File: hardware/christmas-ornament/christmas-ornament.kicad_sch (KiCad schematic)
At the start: 21 parts, among them SW1 SW_Push, U1 ATtiny84A-SS

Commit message: designed basic pcb shape and routing (not finished)
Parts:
- added J1, J2, J3, J4, J5: Conn_01x01_Pin, TestPoint:TestPoint_Pad_D1.5mm, symbol Connector:Conn_01x01_Pin
- BT1: footprint (none) -> Battery:BatteryHolder_Keystone_1060_1x2032
- C1, C2: footprint (none) -> Capacitor_SMD:C_0805_2012Metric
- D1, D2, D3, D4, D5, D6, D7, D8: footprint (none) -> LED_THT:LED_D5.0mm
- R1, R2, R3, R4, R5, R6, R7, R8: footprint (none) -> Resistor_SMD:R_0805_2012Metric
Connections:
- net GND: now also J2.1 (Pin_1)
- net at BT1.1 (+), C1.1, C2.1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: now also J1.1 (Pin_1)
- net at R5.1, R6.1, U1.7 (PA6): now also J3.1 (Pin_1)
- net at U1.4 (~{RESET}/PB3): now also J5.1 (Pin_1)
- net at U1.9 (PA4): now also J4.1 (Pin_1)
- no-connect marks 7 -> 5
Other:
- moved on the sheet: SW1

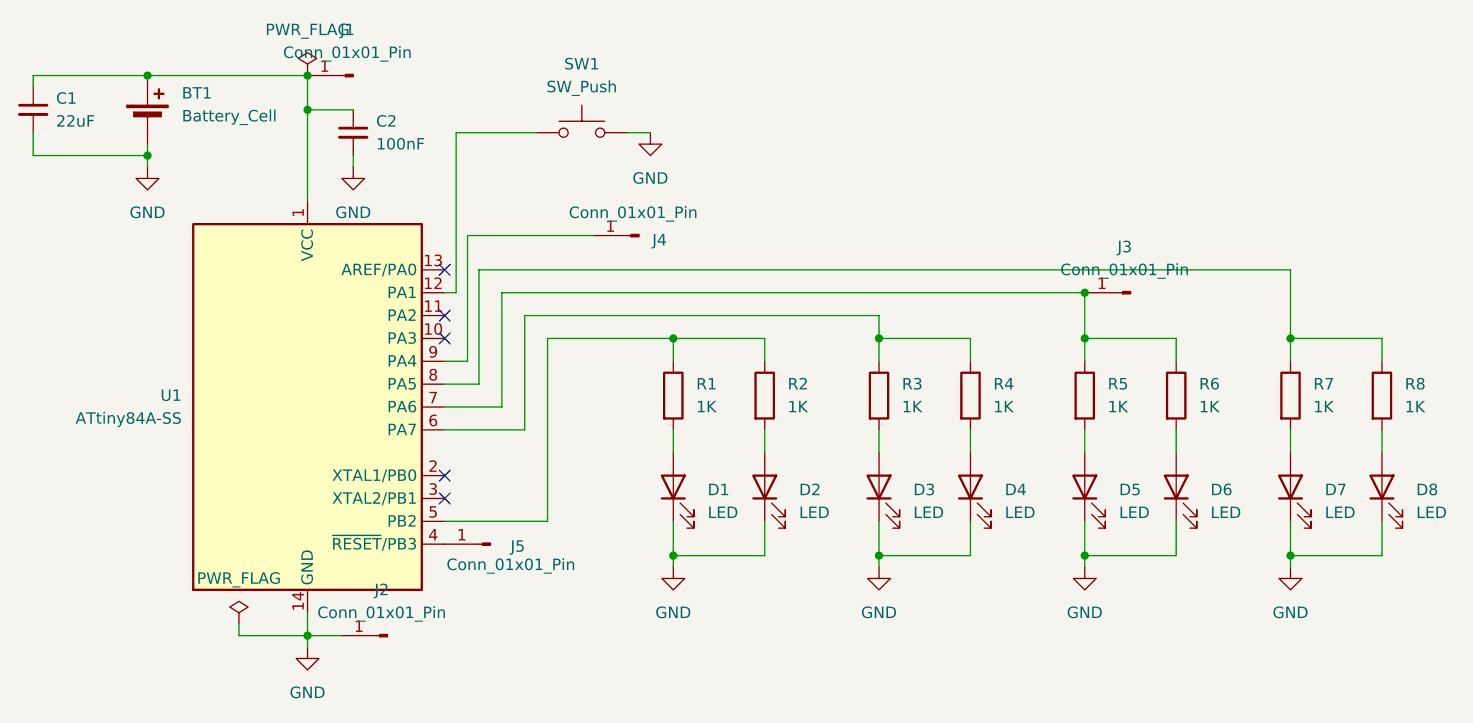
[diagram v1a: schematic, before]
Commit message: improved pcb design
added ground plane (wip?) ; routing basically done
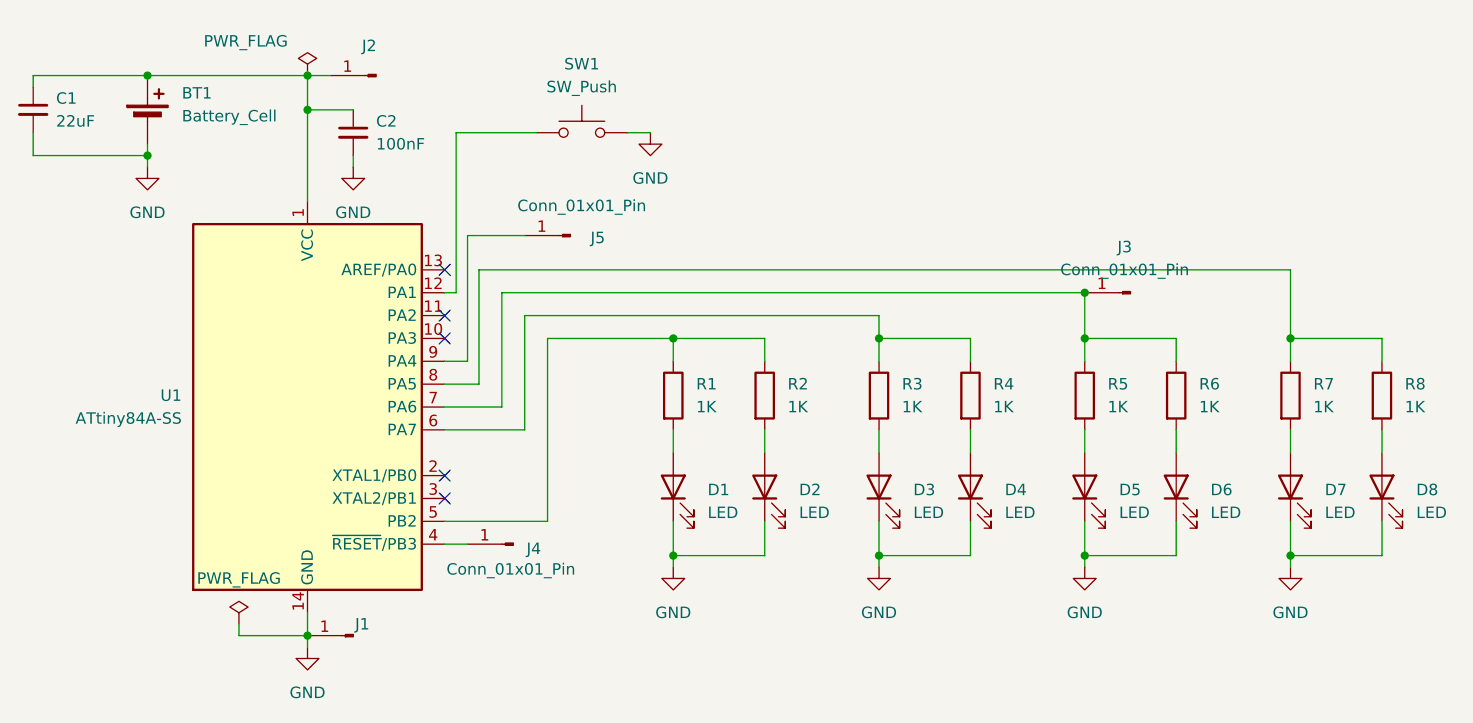
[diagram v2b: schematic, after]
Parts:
- J1: value Conn_01x01_Pin -> (none)
- SW1: footprint (none) -> Button_Switch_SMD:SW_Push_1P1T_NO_CK_KSC6xxJ
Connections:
- net GND: now also J1.1 (Pin_1); no longer J2.1 (Pin_1)
- net at BT1.1 (+), C1.1, C2.1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: now also J2.1 (Pin_1); no longer J1.1 (Pin_1)
- net at J5.1 (Pin_1): now also U1.9 (PA4); no longer U1.4 (~{RESET}/PB3)
- net at J4.1 (Pin_1): now also U1.4 (~{RESET}/PB3); no longer U1.9 (PA4)
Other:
- moved on the sheet: J1, J2, J4, J5
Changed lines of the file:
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@@
-	(wire
-		(pts
-			(xy 107.95 67.31) (xy 121.92 67.31)
-		)
-		(stroke
-			(width 0)
-			(type default)
-		)
-	)
 	(wire
 		(pts
@@
 	(wire
 		(pts
-			(xy 90.17 111.76) (xy 93.98 111.76)
-		)
-		(stroke
-			(width 0)
-			(type default)
-		)
-	)
-	(wire
-		(pts
 			(xy 130.81 102.87) (xy 130.81 104.14)
 		)
@@
 	(wire
 		(pts
+			(xy 107.95 67.31) (xy 114.3 67.31)
+		)
+		(stroke
+			(width 0)
+			(type default)
+		)
+	)
+	(wire
+		(pts
 			(xy 90.17 113.03) (xy 90.17 111.76)
 		)
@@
 	(wire
 		(pts
+			(xy 105.41 101.6) (xy 107.95 101.6)
+		)
+		(stroke
+			(width 0)
+			(type default)
+		)
+	)
+	(wire
+		(pts
 			(xy 153.67 78.74) (xy 153.67 81.28)
 		)
@@
 		(pts
 			(xy 176.53 88.9) (xy 176.53 91.44)
+		)
+		(stroke
+			(width 0)
+			(type default)
+		)
+	)
+	(wire
+		(pts
+			(xy 90.17 49.53) (xy 92.71 49.53)
 		)
 		(stroke
@@
 	(symbol
 		(lib_id "Connector:Conn_01x01_Pin")
-		(at 99.06 111.76 180)
+		(at 97.79 49.53 180)
 		(unit 1)
 		(body_style 1)
@@
 		(in_pos_files yes)
 		(dnp no)
-		(fields_autoplaced yes)
 		(property "Reference" "J2"
-			(at 98.425 106.68 0)
+			(at 97.028 46.228 0)
 			(show_name no)
 			(do_not_autoplace no)
@@
 		)
 		(property "Value" "Conn_01x01_Pin"
-			(at 98.425 109.22 0)
+			(at 97.155 46.99 0)
+			(hide yes)
 			(show_name no)
 			(do_not_autoplace no)
@@
 		)
 		(property "Footprint" "TestPoint:TestPoint_Pad_D1.5mm"
-			(at 99.06 111.76 0)
+			(at 97.79 49.53 0)
 			(hide yes)
 			(show_name no)
@@
 		)
 		(property "Datasheet" ""
-			(at 99.06 111.76 0)
+			(at 97.79 49.53 0)
 			(hide yes)
 			(show_name no)
@@
 		)
 		(property "Description" "Generic connector, single row, 01x01, script generated"
-			(at 99.06 111.76 0)
+			(at 97.79 49.53 0)
 			(hide yes)
 			(show_name no)
@@
 		(in_pos_files yes)
 		(dnp no)
-		(fields_autoplaced yes)
 		(property "Reference" "#FLG01"
 			(at 90.17 47.625 0)
@@
 		)
 		(property "Value" "PWR_FLAG"
-			(at 90.17 44.45 0)
+			(at 83.312 45.72 0)
 			(show_name no)
 			(do_not_autoplace no)
@@
 			)
 		)
-		(property "Footprint" ""
+		(property "Footprint" "Button_Switch_SMD:SW_Push_1P1T_NO_CK_KSC6xxJ"
 			(at 120.65 50.8 0)
 			(hide yes)
@@
 	(symbol
 		(lib_id "Connector:Conn_01x01_Pin")
-		(at 110.49 101.6 180)
+		(at 119.38 67.31 180)
 		(unit 1)
 		(body_style 1)
@@
 		(dnp no)
 		(property "Reference" "J5"
-			(at 113.538 101.854 0)
+			(at 122.428 67.564 0)
 			(show_name no)
 			(do_not_autoplace no)
@@
 		)
 		(property "Value" "Conn_01x01_Pin"
-			(at 112.776 103.886 0)
+			(at 120.65 64.008 0)
 			(show_name no)
 			(do_not_autoplace no)
@@
 		)
 		(property "Footprint" "TestPoint:TestPoint_Pad_D1.5mm"
-			(at 110.49 101.6 0)
+			(at 119.38 67.31 0)
 			(hide yes)
 			(show_name no)
@@
 		)
 		(property "Datasheet" ""
-			(at 110.49 101.6 0)
+			(at 119.38 67.31 0)
 			(hide yes)
 			(show_name no)
@@
 		)
 		(property "Description" "Generic connector, single row, 01x01, script generated"
-			(at 110.49 101.6 0)
+			(at 119.38 67.31 0)
 			(hide yes)
 			(show_name no)
@@
 	(symbol
 		(lib_id "Connector:Conn_01x01_Pin")
-		(at 127 67.31 180)
+		(at 113.03 101.6 180)
 		(unit 1)
 		(body_style 1)
@@
 		(dnp no)
 		(property "Reference" "J4"
-			(at 129.286 67.818 0)
+			(at 115.316 102.108 0)
 			(show_name no)
 			(do_not_autoplace no)
@@
 		)
 		(property "Value" "Conn_01x01_Pin"
-			(at 126.365 64.77 0)
+			(at 112.776 104.394 0)
 			(show_name no)
 			(do_not_autoplace no)
@@
 		)
 		(property "Footprint" "TestPoint:TestPoint_Pad_D1.5mm"
-			(at 127 67.31 0)
+			(at 113.03 101.6 0)
 			(hide yes)
 			(show_name no)
@@
 		)
 		(property "Datasheet" ""
-			(at 127 67.31 0)
+			(at 113.03 101.6 0)
 			(hide yes)
 			(show_name no)
@@
 		)
 		(property "Description" "Generic connector, single row, 01x01, script generated"
-			(at 127 67.31 0)
+			(at 113.03 101.6 0)
 			(hide yes)
 			(show_name no)
@@
 	(symbol
 		(lib_id "Connector:Conn_01x01_Pin")
-		(at 95.25 49.53 180)
+		(at 95.25 111.76 180)
 		(unit 1)
 		(body_style 1)
@@
 		(in_pos_files yes)
 		(dnp no)
-		(fields_autoplaced yes)
 		(property "Reference" "J1"
-			(at 94.615 44.45 0)
-			(show_name no)
-			(do_not_autoplace no)
-			(effects
-				(font
-					(size 1.27 1.27)
-				)
-			)
-		)
-		(property "Value" "Conn_01x01_Pin"
-			(at 94.615 46.99 0)
+			(at 96.266 110.49 0)
+			(show_name no)
+			(do_not_autoplace no)
+			(effects
+				(font
+					(size 1.27 1.27)
+				)
+			)
+		)
+		(property "Value" ""
+			(at 94.615 109.22 0)
 			(show_name no)
 			(do_not_autoplace no)
@@
 		)
 		(property "Footprint" "TestPoint:TestPoint_Pad_D1.5mm"
-			(at 95.25 49.53 0)
+			(at 95.25 111.76 0)
 			(hide yes)
 			(show_name no)
@@
 		)
 		(property "Datasheet" ""
-			(at 95.25 49.53 0)
+			(at 95.25 111.76 0)
 			(hide yes)
 			(show_name no)
@@
 		)
 		(property "Description" "Generic connector, single row, 01x01, script generated"
-			(at 95.25 49.53 0)
-			(hide yes)
-			(show_name no)
+			(at 95.25 111.76 0)
+			(hide yes)
+			(show_name no)
